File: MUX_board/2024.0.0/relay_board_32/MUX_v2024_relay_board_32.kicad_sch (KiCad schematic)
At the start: 19 parts, among them J1 Relays Pwr, J2 I2C, J3 Screw_Terminal_01x04, J4 Conn_02x08_Odd_Even, J5 Screw_Terminal_01x16, U1 MCP23017_SP, U2 MCP23017_SP

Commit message: Updates footprints
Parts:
- J1: footprint TerminalBlock_Phoenix:TerminalBlock_Phoenix_MKDS-1,5-2_1x02_P5.00mm_Horizontal -> TerminalBlock_Phoenix:TerminalBlock_Phoenix_MKDS-1,5-2-5.08_1x02_P5.08mm_Horizontal
- J3: footprint TerminalBlock_Phoenix:TerminalBlock_Phoenix_MKDS-1,5-4_1x04_P5.00mm_Horizontal -> TerminalBlock_Phoenix:TerminalBlock_Phoenix_MKDS-1,5-5-5.08_1x05_P5.08mm_Horizontal
- J5: footprint TerminalBlock_Phoenix:TerminalBlock_Phoenix_MKDS-1,5-16_1x16_P5.00mm_Horizontal -> TerminalBlock_Phoenix:TerminalBlock_Phoenix_MKDS-1,5-16-5.08_1x16_P5.08mm_Horizontal
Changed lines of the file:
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@@
     (property "Reference" "J3" (id 0) (at 44.45 170.18 90))
     (property "Value" "Screw_Terminal_01x04" (id 1) (at 44.45 172.72 90))
-    (property "Footprint" "TerminalBlock_Phoenix:TerminalBlock_Phoenix_MKDS-1,5-4_1x04_P5.00mm_Horizontal" (id 2) (at 43.18 177.165 0)
+    (property "Footprint" "TerminalBlock_Phoenix:TerminalBlock_Phoenix_MKDS-1,5-5-5.08_1x05_P5.08mm_Horizontal" (id 2) (at 43.18 177.165 0)
       (effects (font (size 1.27 1.27)) hide)
     )
@@
       (effects (font (size 1.27 1.27)) (justify left))
     )
-    (property "Footprint" "TerminalBlock_Phoenix:TerminalBlock_Phoenix_MKDS-1,5-2_1x02_P5.00mm_Horizontal" (id 2) (at 25.4 126.365 0)
+    (property "Footprint" "TerminalBlock_Phoenix:TerminalBlock_Phoenix_MKDS-1,5-2-5.08_1x02_P5.08mm_Horizontal" (id 2) (at 25.4 126.365 0)
       (effects (font (size 1.27 1.27)) hide)
     )
@@
     (property "Reference" "J5" (id 0) (at 154.305 208.28 90))
     (property "Value" "Screw_Terminal_01x16" (id 1) (at 154.305 210.82 90))
-    (property "Footprint" "TerminalBlock_Phoenix:TerminalBlock_Phoenix_MKDS-1,5-16_1x16_P5.00mm_Horizontal" (id 2) (at 153.035 215.265 0)
+    (property "Footprint" "TerminalBlock_Phoenix:TerminalBlock_Phoenix_MKDS-1,5-16-5.08_1x16_P5.08mm_Horizontal" (id 2) (at 153.035 215.265 0)
       (effects (font (size 1.27 1.27)) hide)
     )
@@
     )
     (path "/c416053f-73b6-4985-bb42-db33da63c80a"
-      (reference "J1") (unit 1) (value "Relays Pwr") (footprint "TerminalBlock_Phoenix:TerminalBlock_Phoenix_MKDS-1,5-2_1x02_P5.00mm_Horizontal")
+      (reference "J1") (unit 1) (value "Relays Pwr") (footprint "TerminalBlock_Phoenix:TerminalBlock_Phoenix_MKDS-1,5-2-5.08_1x02_P5.08mm_Horizontal")
     )
     (path "/27027fc7-0ffe-414c-81cd-d00be9c60ed1"
@@
     )
     (path "/8151541a-a38e-4a24-8b78-b568069f5f2d"
-      (reference "J3") (unit 1) (value "Screw_Terminal_01x04") (footprint "TerminalBlock_Phoenix:TerminalBlock_Phoenix_MKDS-1,5-4_1x04_P5.00mm_Horizontal")
+      (reference "J3") (unit 1) (value "Screw_Terminal_01x04") (footprint "TerminalBlock_Phoenix:TerminalBlock_Phoenix_MKDS-1,5-5-5.08_1x05_P5.08mm_Horizontal")
     )
     (path "/13d5b8a6-8ed6-49ce-95a4-239de8600b7a"
@@
     )
     (path "/f1801d73-c5ef-4ad8-b05f-5217ff13ffce"
-      (reference "J5") (unit 1) (value "Screw_Terminal_01x16") (footprint "TerminalBlock_Phoenix:TerminalBlock_Phoenix_MKDS-1,5-16_1x16_P5.00mm_Horizontal")
+      (reference "J5") (unit 1) (value "Screw_Terminal_01x16") (footprint "TerminalBlock_Phoenix:TerminalBlock_Phoenix_MKDS-1,5-16-5.08_1x16_P5.08mm_Horizontal")
     )
     (path "/fe10c99a-9c56-4111-8450-4fe288599c36"

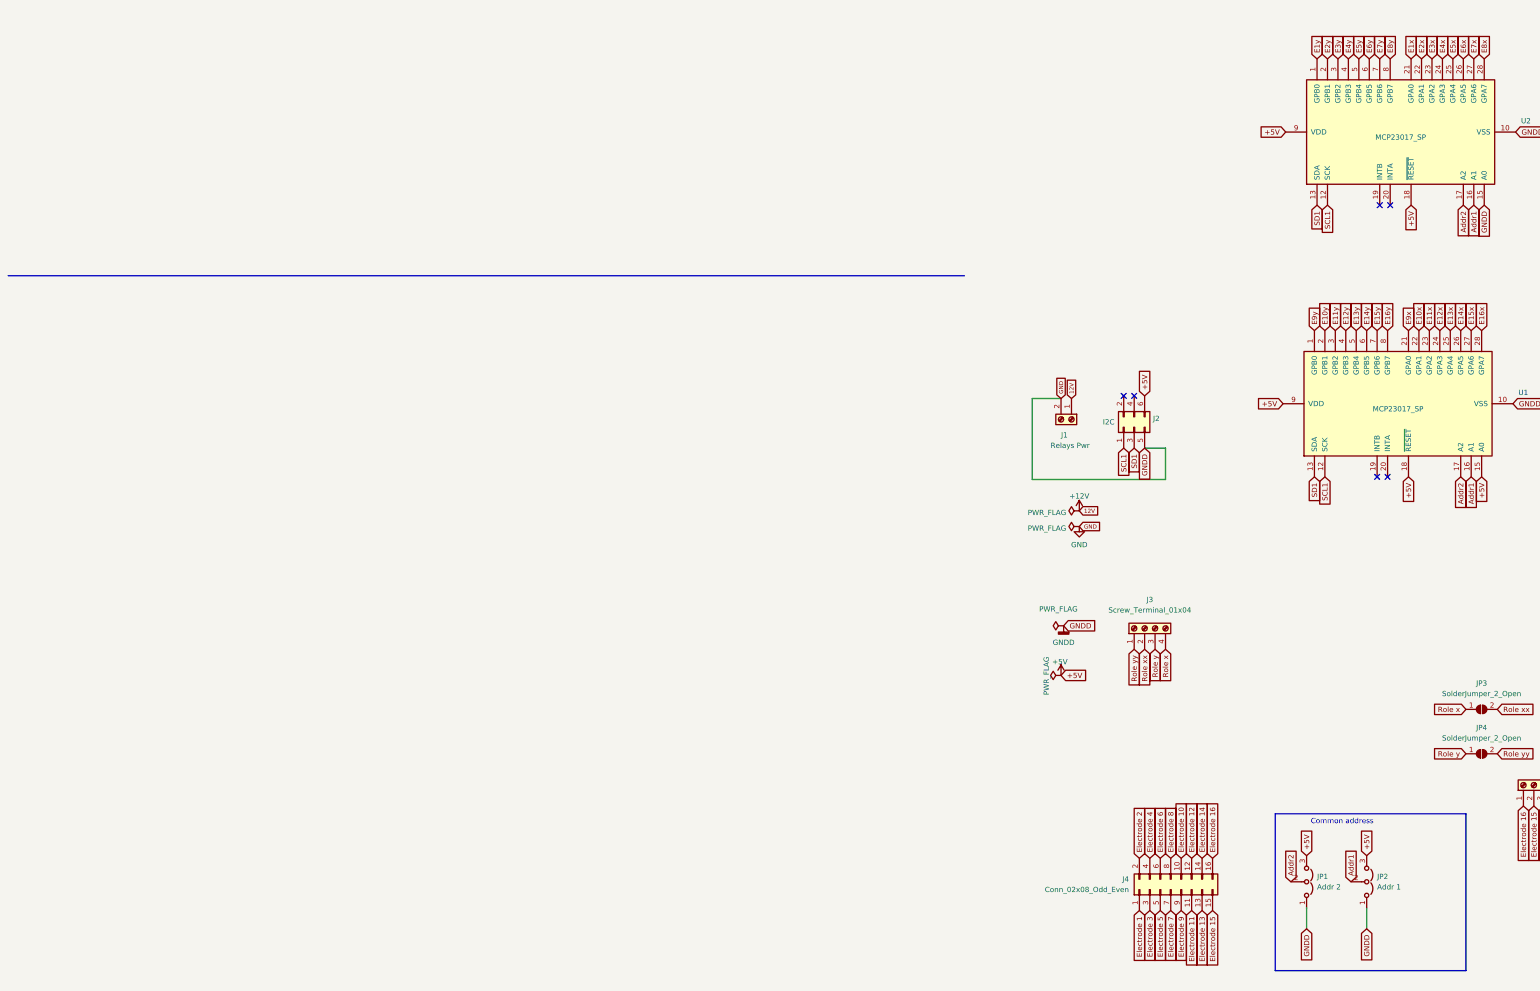
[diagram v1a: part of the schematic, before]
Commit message: Adds capacitor on MCP
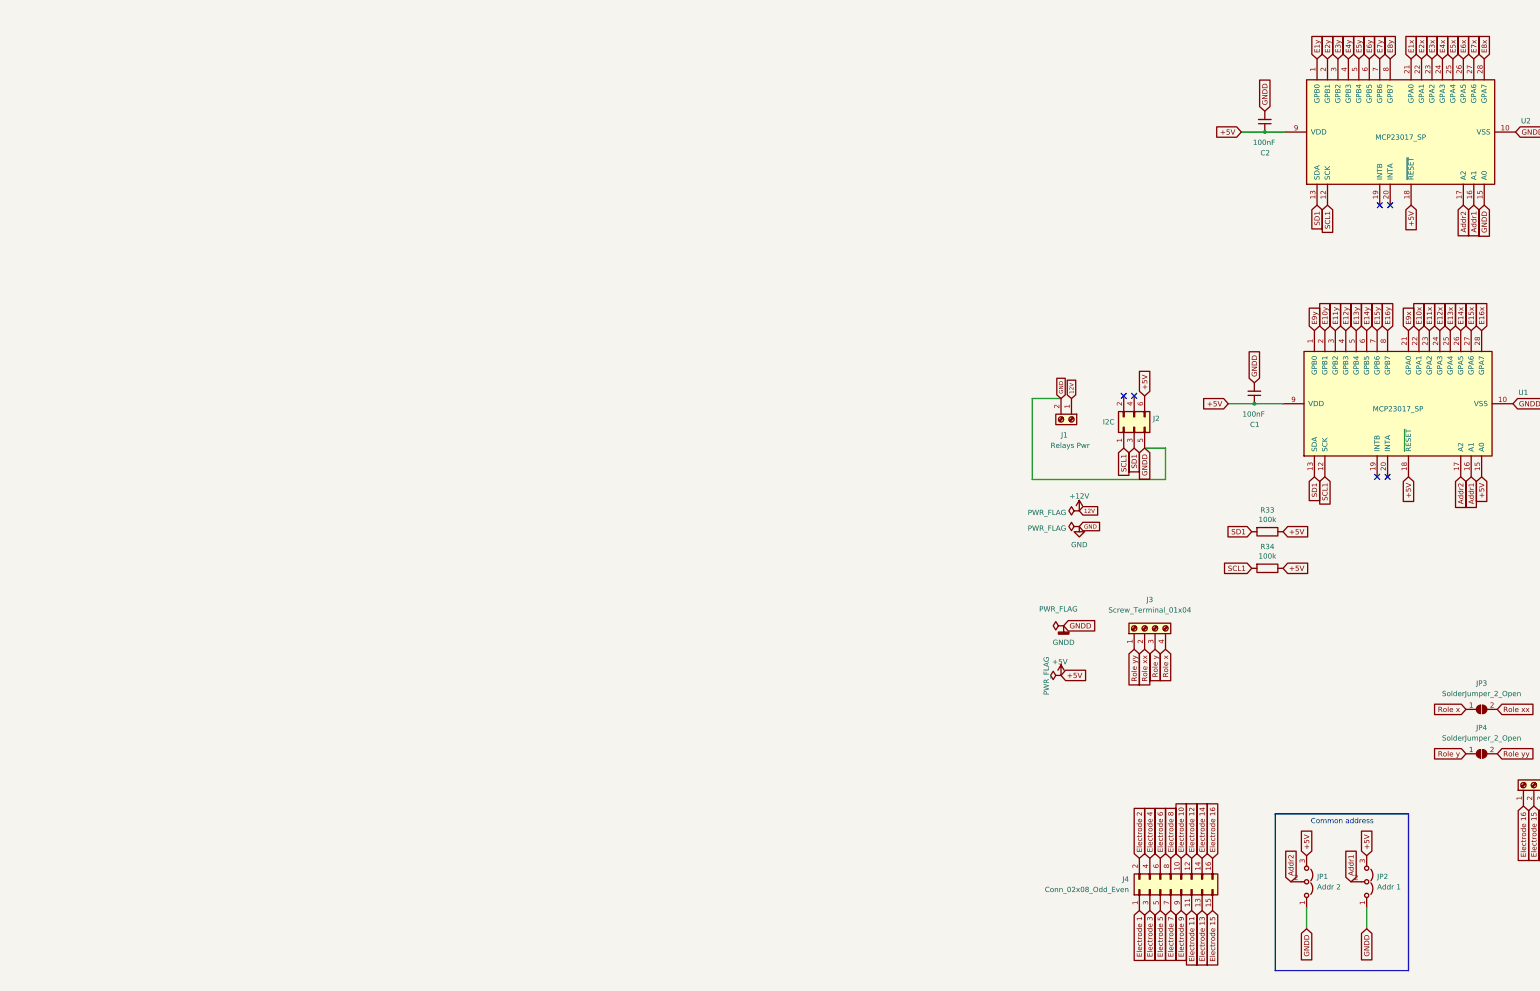
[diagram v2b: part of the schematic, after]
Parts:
- added C1, C2: 100nF, Capacitor_THT:C_Disc_D8.0mm_W2.5mm_P5.00mm, symbol Device:C_Small
- added R33, R34: 100k, Resistor_THT:R_Axial_DIN0207_L6.3mm_D2.5mm_P15.24mm_Horizontal, symbol Device:R
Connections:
- net +5V: now also C1.1, C2.1, R33.1, R34.1
- net GND: now also C1.2, C2.2
- net SCL1: now also R34.2
- net SD1: now also R33.2
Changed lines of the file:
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@@
   (junction (at 240.03 127) (diameter 0) (color 0 0 0 0)
   )
+  (junction (at 69.85 122.555) (diameter 0) (color 0 0 0 0)
+  )
   (junction (at 348.615 111.76) (diameter 0) (color 0 0 0 0)
   )
@@
   (junction (at 294.64 43.18) (diameter 0) (color 0 0 0 0)
   )
+  (junction (at 72.39 56.515) (diameter 0) (color 0 0 0 0)
+  )
   (junction (at 348.615 127) (diameter 0) (color 0 0 0 0)
   )
@@
     (stroke (width 0) (type default) (color 0 0 0 0))
   )
-  (polyline (pts (xy 74.93 260.35) (xy 121.285 260.35))
+  (polyline (pts (xy 74.93 260.35) (xy 107.315 260.35))
     (stroke (width 0) (type default) (color 0 0 0 0))
   )
@@
     (stroke (width 0) (type default) (color 0 0 0 0))
   )
-  (polyline (pts (xy -0.635 91.44) (xy -233.045 91.44))
+  (wire (pts (xy 240.03 57.785) (xy 240.03 42.545))
     (stroke (width 0) (type default) (color 0 0 0 0))
   )
-  (wire (pts (xy 240.03 57.785) (xy 240.03 42.545))
+  (wire (pts (xy 72.39 56.515) (xy 77.47 56.515))
     (stroke (width 0) (type default) (color 0 0 0 0))
   )
@@
     (stroke (width 0) (type default) (color 0 0 0 0))
   )
-  (polyline (pts (xy 121.285 260.35) (xy 121.285 222.25))
+  (polyline (pts (xy 107.315 260.35) (xy 107.315 222.25))
     (stroke (width 0) (type default) (color 0 0 0 0))
   )
@@
     (stroke (width 0) (type default) (color 0 0 0 0))
   )
+  (wire (pts (xy 69.85 122.555) (xy 76.835 122.555))
+    (stroke (width 0) (type default) (color 0 0 0 0))
+  )
   (wire (pts (xy 240.03 127) (xy 240.03 111.76))
     (stroke (width 0) (type default) (color 0 0 0 0))
@@
     (stroke (width 0) (type default) (color 0 0 0 0))
   )
-  (polyline (pts (xy 121.285 222.25) (xy 74.93 222.25))
+  (polyline (pts (xy 107.315 222.25) (xy 74.93 222.25))
     (stroke (width 0) (type default) (color 0 0 0 0))
   )
@@
     (stroke (width 0) (type default) (color 0 0 0 0))
   )
+  (wire (pts (xy 66.675 56.515) (xy 72.39 56.515))
+    (stroke (width 0) (type default) (color 0 0 0 0))
+  )
   (wire (pts (xy 213.995 110.49) (xy 220.345 110.49))
     (stroke (width 0) (type default) (color 0 0 0 0))
@@
     (stroke (width 0) (type default) (color 0 0 0 0))
   )
+  (wire (pts (xy 63.5 122.555) (xy 69.85 122.555))
+    (stroke (width 0) (type default) (color 0 0 0 0))
+  )
   (wire (pts (xy 186.055 43.18) (xy 192.405 43.18))
     (stroke (width 0) (type default) (color 0 0 0 0))
@@
     (effects (font (size 1.27 1.27)) (justify left bottom))
   )
-  (global_label "+5V" (shape input) (at 76.835 122.555 180) (fields_autoplaced)
+  (global_label "+5V" (shape input) (at 63.5 122.555 180) (fields_autoplaced)
     (effects (font (size 1.27 1.27)) (justify right))
-    (property "Intersheet References" "${INTERSHEET_REFS}" (id 0) (at 70.6403 122.6344 0)
+    (property "Intersheet References" "${INTERSHEET_REFS}" (id 0) (at 57.3053 122.6344 0)
       (effects (font (size 1.27 1.27)) (justify right) hide)
     )
@@
     )
   )
+  (global_label "+5V" (shape input) (at 76.835 153.67 0) (fields_autoplaced)
+    (effects (font (size 1.27 1.27)) (justify left))
+    (property "Intersheet References" "${INTERSHEET_REFS}" (id 0) (at 83.0297 153.5906 0)
+      (effects (font (size 1.27 1.27)) (justify left) hide)
+    )
+  )
   (global_label "E6x" (shape input) (at 120.65 38.735 90) (fields_autoplaced)
     (effects (font (size 1.27 1.27)) (justify left))
@@
     )
   )
+  (global_label "SD1" (shape input) (at 69.215 153.67 180) (fields_autoplaced)
+    (effects (font (size 1.27 1.27)) (justify right))
+    (property "Intersheet References" "${INTERSHEET_REFS}" (id 0) (at 61.1456 153.5906 0)
+      (effects (font (size 1.27 1.27)) (justify right) hide)
+    )
+  )
   (global_label "Electrode 5" (shape input) (at 192.405 93.98 180) (fields_autoplaced)
     (effects (font (size 1.27 1.27)) (justify right))
@@
     )
   )
+  (global_label "SCL1" (shape input) (at 69.215 162.56 180) (fields_autoplaced)
+    (effects (font (size 1.27 1.27)) (justify right))
+    (property "Intersheet References" "${INTERSHEET_REFS}" (id 0) (at 62.1737 162.6394 0)
+      (effects (font (size 1.27 1.27)) (justify right) hide)
+    )
+  )
   (global_label "Electrode 9" (shape input) (at 52.07 245.745 270) (fields_autoplaced)
     (effects (font (size 1.27 1.27)) (justify right))
@@
     )
   )
+  (global_label "GNDD" (shape input) (at 72.39 51.435 90) (fields_autoplaced)
+    (effects (font (size 1.27 1.27)) (justify left))
+    (property "Intersheet References" "${INTERSHEET_REFS}" (id 0) (at 72.3106 43.9703 90)
+      (effects (font (size 1.27 1.27)) (justify left) hide)
+    )
+  )
   (global_label "E9y" (shape input) (at 384.81 23.495 0) (fields_autoplaced)
     (effects (font (size 1.27 1.27)) (justify left))
@@
     )
   )
-  (global_label "+5V" (shape input) (at 77.47 56.515 180) (fields_autoplaced)
+  (global_label "+5V" (shape input) (at 66.675 56.515 180) (fields_autoplaced)
     (effects (font (size 1.27 1.27)) (justify right))
-    (property "Intersheet References" "${INTERSHEET_REFS}" (id 0) (at 71.2753 56.5944 0)
+    (property "Intersheet References" "${INTERSHEET_REFS}" (id 0) (at 60.4803 56.5944 0)
       (effects (font (size 1.27 1.27)) (justify right) hide)
     )
@@
     )
   )
+  (global_label "+5V" (shape input) (at 76.835 162.56 0) (fields_autoplaced)
+    (effects (font (size 1.27 1.27)) (justify left))
+    (property "Intersheet References" "${INTERSHEET_REFS}" (id 0) (at 83.0297 162.4806 0)
+      (effects (font (size 1.27 1.27)) (justify left) hide)
+    )
+  )
+  (global_label "GNDD" (shape input) (at 69.85 117.475 90) (fields_autoplaced)
+    (effects (font (size 1.27 1.27)) (justify left))
+    (property "Intersheet References" "${INTERSHEET_REFS}" (id 0) (at 69.7706 110.0103 90)
+      (effects (font (size 1.27 1.27)) (justify left) hide)
+    )
+  )
   (global_label "Electrode 8" (shape input) (at 192.405 139.7 180) (fields_autoplaced)
     (effects (font (size 1.27 1.27)) (justify right))
@@
     (pin "6")
   )
+  (symbol (lib_id "Device:C_Small") (at 72.39 53.975 180) (unit 1)
+    (in_bom yes) (on_board yes)
+    (property "Reference" "C2" (id 0) (at 73.66 61.595 0)
+      (effects (font (size 1.27 1.27)) (justify left))
+    )
+    (property "Value" "100nF" (id 1) (at 74.93 59.055 0)
+      (effects (font (size 1.27 1.27)) (justify left))
+    )
+    (property "Footprint" "Capacitor_THT:C_Disc_D8.0mm_W2.5mm_P5.00mm" (id 2) (at 72.39 53.975 0)
+      (effects (font (size 1.27 1.27)) hide)
+    )
+    (property "Datasheet" "~" (id 3) (at 72.39 53.975 0)
+      (effects (font (size 1.27 1.27)) hide)
+    )
+    (pin "1")
+    (pin "2")
+  )
   (symbol (lib_id "Jumper:SolderJumper_2_Open") (at 267.335 243.84 0) (unit 1)
     (in_bom yes) (on_board yes) (fields_autoplaced)
@@
     (pin "2")
   )
+  (symbol (lib_id "Device:C_Small") (at 69.85 120.015 180) (unit 1)
+    (in_bom yes) (on_board yes)
+    (property "Reference" "C1" (id 0) (at 71.12 127.635 0)
+      (effects (font (size 1.27 1.27)) (justify left))
+    )
+    (property "Value" "100nF" (id 1) (at 72.39 125.095 0)
+      (effects (font (size 1.27 1.27)) (justify left))
+    )
+    (property "Footprint" "Capacitor_THT:C_Disc_D8.0mm_W2.5mm_P5.00mm" (id 2) (at 69.85 120.015 0)
+      (effects (font (size 1.27 1.27)) hide)
+    )
+    (property "Datasheet" "~" (id 3) (at 69.85 120.015 0)
+      (effects (font (size 1.27 1.27)) hide)
+    )
+    (pin "1")
+    (pin "2")
+  )
+  (symbol (lib_id "Device:R") (at 73.025 162.56 270) (unit 1)
+    (in_bom yes) (on_board yes)
+    (property "Reference" "R34" (id 0) (at 73.025 157.3022 90))
+    (property "Value" "100k" (id 1) (at 73.025 159.6136 90))
+    (property "Footprint" "Resistor_THT:R_Axial_DIN0207_L6.3mm_D2.5mm_P15.24mm_Horizontal" (id 2) (at 73.025 160.782 90)
+      (effects (font (size 1.27 1.27)) hide)
+    )
+    (property "Datasheet" "~" (id 3) (at 73.025 162.56 0)
+      (effects (font (size 1.27 1.27)) hide)
+    )
+    (pin "1")
+    (pin "2")
+  )
   (symbol (lib_id "power:+12V") (at 27.305 148.59 0) (unit 1)
     (in_bom yes) (on_board yes) (fields_autoplaced)
@@
     (pin "2")
   )
+  (symbol (lib_id "Device:R") (at 73.025 153.67 270) (unit 1)
+    (in_bom yes) (on_board yes)
+    (property "Reference" "R33" (id 0) (at 73.025 148.4122 90))
+    (property "Value" "100k" (id 1) (at 73.025 150.7236 90))
+    (property "Footprint" "Resistor_THT:R_Axial_DIN0207_L6.3mm_D2.5mm_P15.24mm_Horizontal" (id 2) (at 73.025 151.892 90)
+      (effects (font (size 1.27 1.27)) hide)
+    )
+    (property "Datasheet" "~" (id 3) (at 73.025 153.67 0)
+      (effects (font (size 1.27 1.27)) hide)
+    )
+    (pin "1")
+    (pin "2")
+  )
   (symbol (lib_id "Jumper:SolderJumper_2_Open") (at 267.335 234.315 0) (unit 1)
     (in_bom yes) (on_board yes) (fields_autoplaced)
@@
       (reference "#PWR04") (unit 1) (value "GND") (footprint "")
     )
+    (path "/4c99bbb8-e08a-4485-a034-a4471d5dafb7"
+      (reference "C1") (unit 1) (value "100nF") (footprint "Capacitor_THT:C_Disc_D8.0mm_W2.5mm_P5.00mm")
+    )
+    (path "/2e9aa831-9ec0-4862-ae14-c35fffc78af7"
+      (reference "C2") (unit 1) (value "100nF") (footprint "Capacitor_THT:C_Disc_D8.0mm_W2.5mm_P5.00mm")
+    )
     (path "/202557b3-1d57-491a-8c53-22fb6f02d7ed/00000000-0000-0000-0000-000062873f4c"
       (reference "D1") (unit 1) (value "1N_E4007") (footprint "Diode_THT:D_DO-41_SOD81_P10.16mm_Horizontal")
@@
       (reference "R32") (unit 1) (value "100k") (footprint "Resistor_THT:R_Axial_DIN0207_L6.3mm_D2.5mm_P15.24mm_Horizontal")
     )
+    (path "/c53fa6a5-8d5b-4549-8d96-7860e8065d41"
+      (reference "R33") (unit 1) (value "100k") (footprint "Resistor_THT:R_Axial_DIN0207_L6.3mm_D2.5mm_P15.24mm_Horizontal")
+    )
+    (path "/5db9106d-b510-4112-a294-6e91b3b12ef0"
+      (reference "R34") (unit 1) (value "100k") (footprint "Resistor_THT:R_Axial_DIN0207_L6.3mm_D2.5mm_P15.24mm_Horizontal")
+    )
     (path "/9d836177-794d-46f3-9ef7-3d778e8cdca5"
